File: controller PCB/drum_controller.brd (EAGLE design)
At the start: 160 x 100 mm, 1 part

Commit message: connected LED anode to +5V
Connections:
- new net +5V: LED1.A
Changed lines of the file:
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@@
 <contactref element="LED1" pad="K"/>
+</signal>
+<signal name="+5V">
+<contactref element="LED1" pad="A"/>
 </signal>
 </signals>

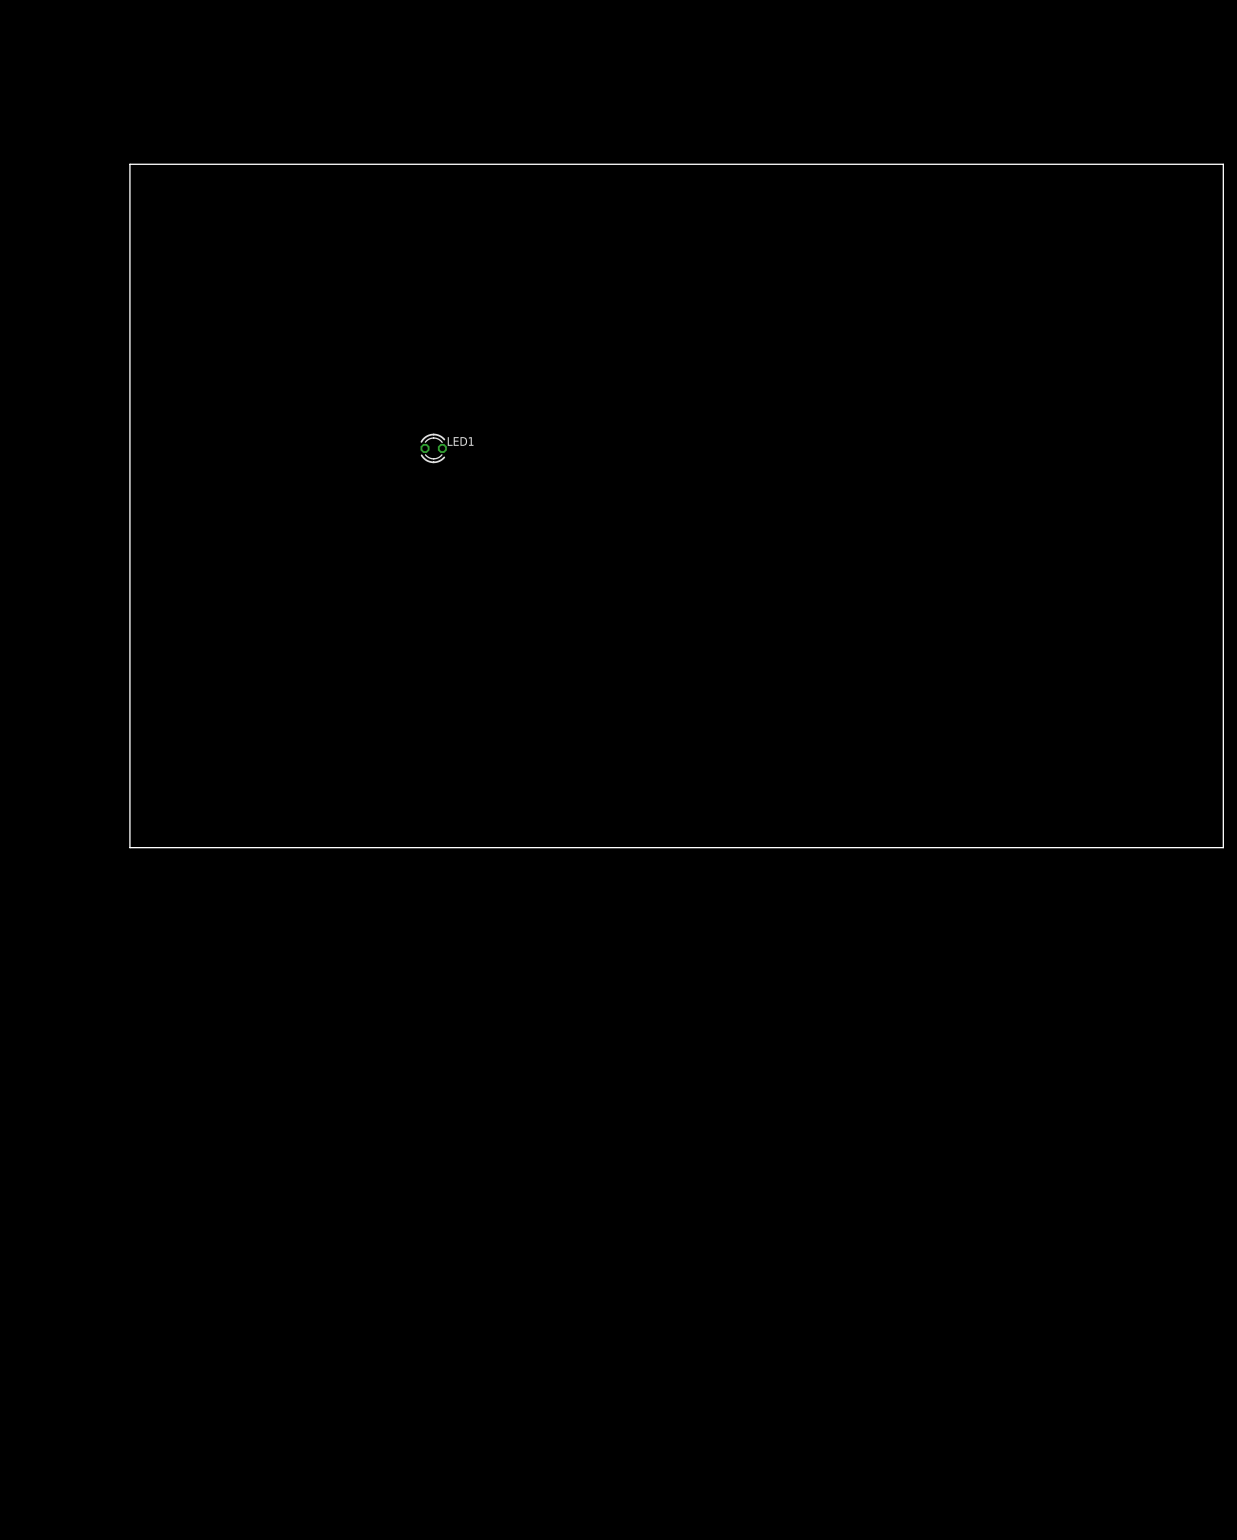
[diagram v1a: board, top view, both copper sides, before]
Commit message: added all 8 piezos to schematic, board not layed out yet
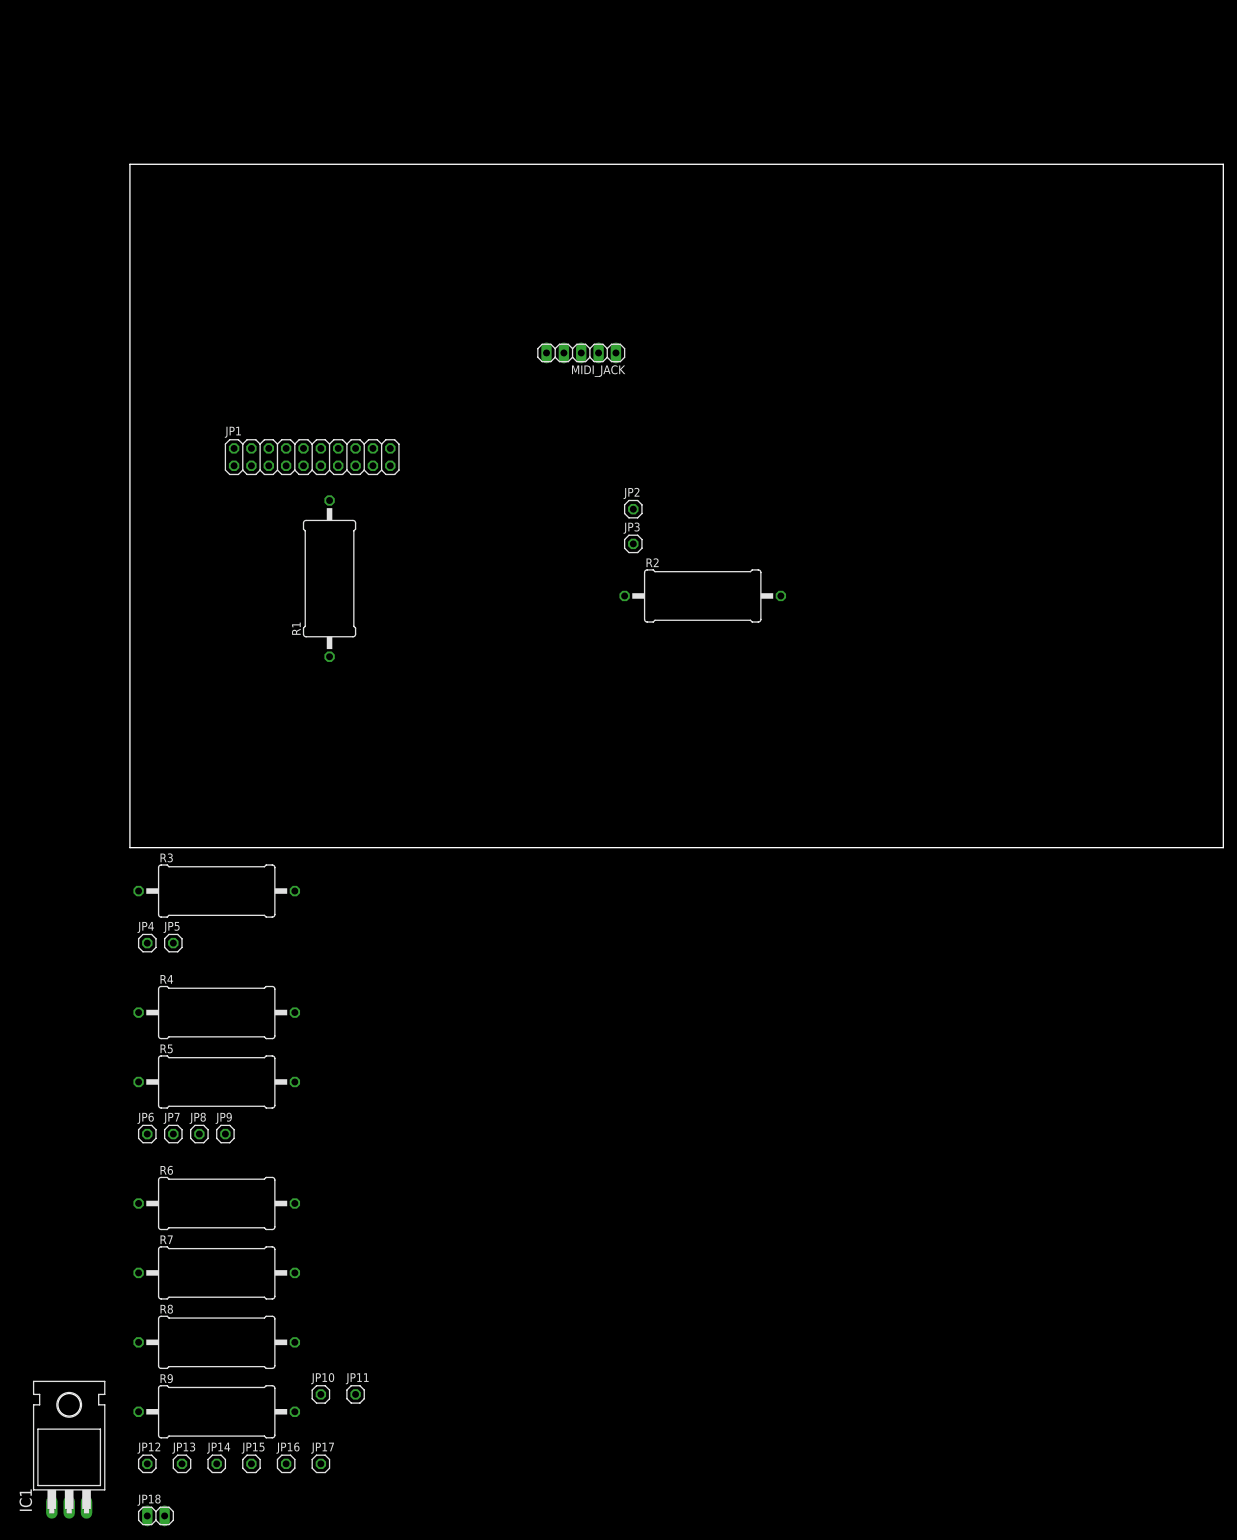
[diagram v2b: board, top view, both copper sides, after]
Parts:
- removed LED1: TLLY4400, led:LED3MM
- added IC1: 7805T, adafruit:TO220H
- added JP1: (no value), pinhead:2X10
- added JP10, JP12, JP14, JP16, JP2, JP4, JP6, JP8: P+, pinhead:1X01
- added JP11, JP13, JP15, JP17, JP3, JP5, JP7, JP9: P-, pinhead:1X01
- added JP18: (no value), pinhead:1X02
- added MIDI_JACK: (no value), pinhead:1X05
- added R1: 220, rcl:P0817/22
- added R2, R3, R4, R5, R6, R7, R8, R9: 1M, rcl:P0817/22
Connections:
- new net 12V: IC1.1, JP18.1
- new net A0: JP1.5, JP2.1, R2.2
- new net A1: JP1.7, JP4.1, R3.2
- new net A2: JP1.9, JP6.1, R4.2
- new net A3: JP1.11, JP8.1, R5.2
- new net A4: JP1.13, JP10.1, R6.2
- new net A5: JP1.15, JP12.1, R7.2
- new net A6: JP1.17, JP14.1, R8.2
- new net A7: JP1.2, JP16.1, R9.2
- new net N$1: MIDI_JACK.4, R1.1
- new net TXD: JP1.3, MIDI_JACK.2
- net +5V: now also IC1.3, JP1.1, R1.2; no longer LED1.A
- net GND: now also IC1.2, JP1.19, JP11.1, JP13.1, JP15.1, JP17.1, JP18.2, JP3.1, JP5.1, JP7.1, JP9.1, MIDI_JACK.3, R2.1, R3.1, R4.1, R5.1, R6.1, R7.1, R8.1, R9.1; no longer LED1.K

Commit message: resized PCB to match Hammond 1898 enclosure (notches need to be completed)
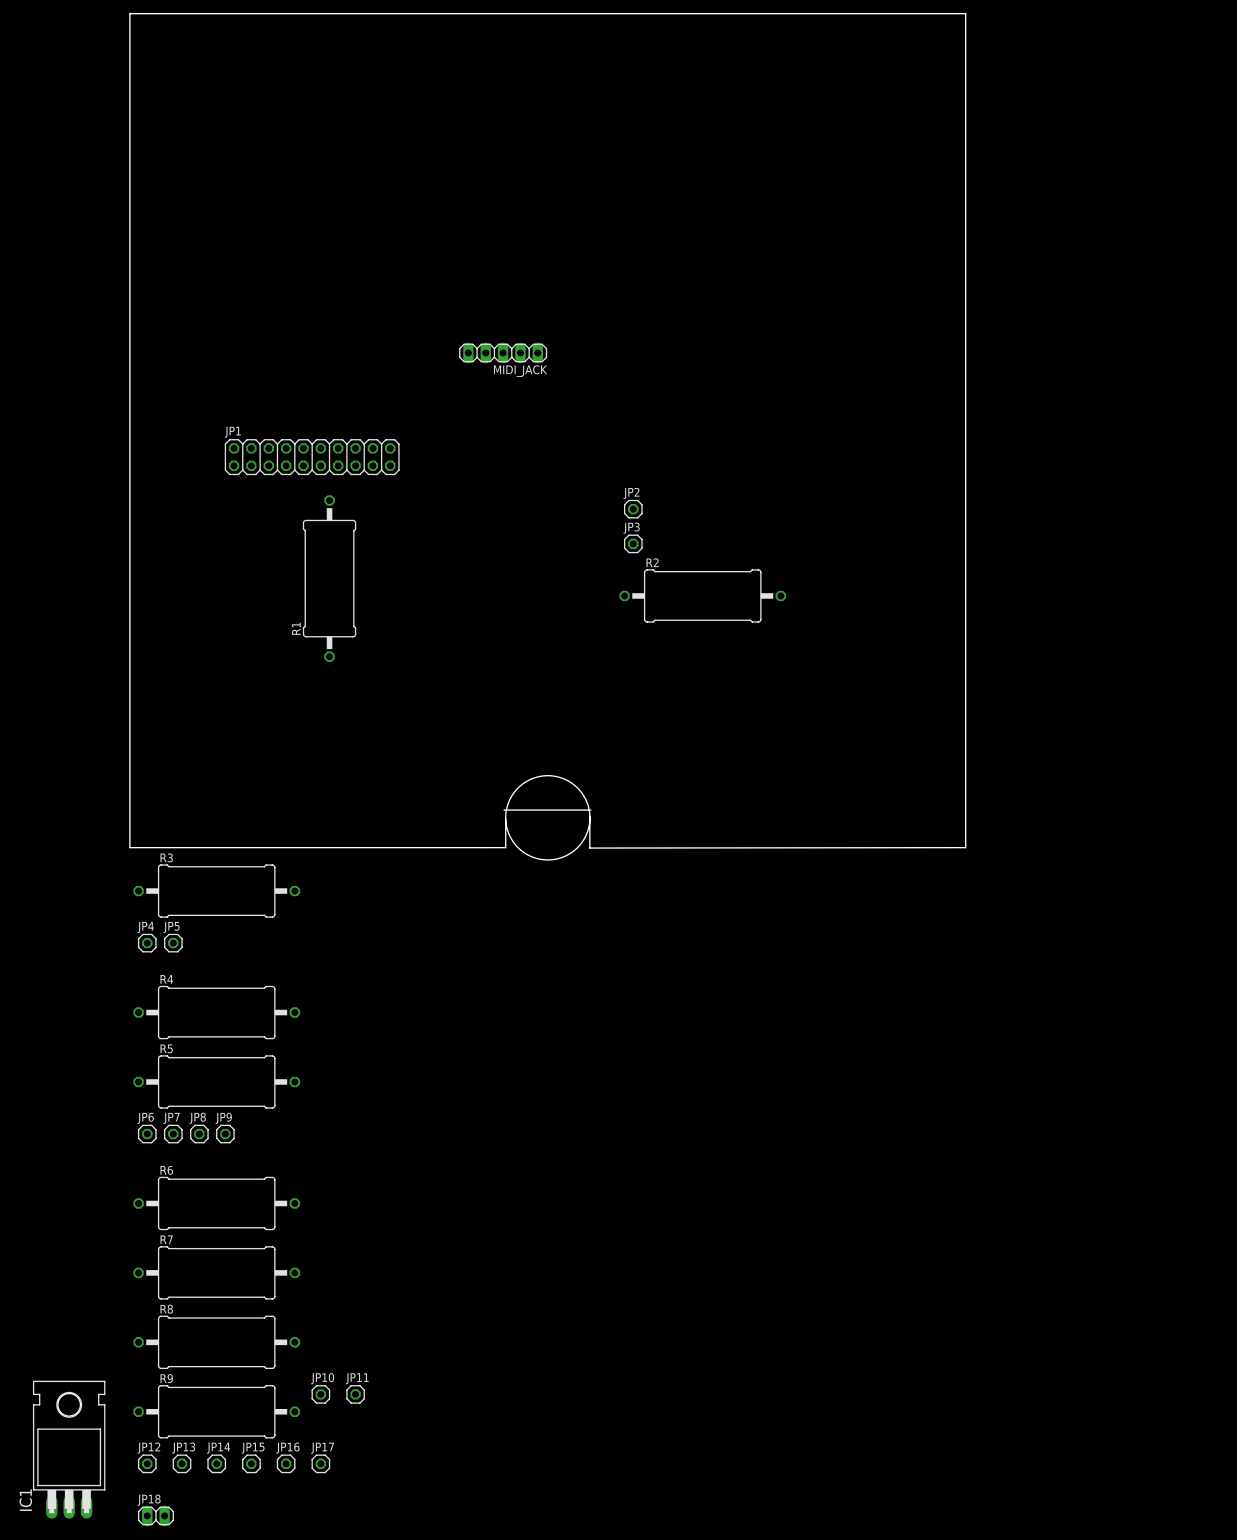
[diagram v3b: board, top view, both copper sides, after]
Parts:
- moved MIDI_JACK 11.4 mm to (54.6, 72.4)
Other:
- board size 160 x 100 mm -> 122.3 x 123.8 mm
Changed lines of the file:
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@@
 <setting verticaltext="up"/>
 </settings>
-<grid distance="50" unitdist="mil" unit="mil" style="lines" multiple="1" display="no" altdistance="5" altunitdist="mil" altunit="mil"/>
+<grid distance="50" unitdist="mil" unit="mm" style="lines" multiple="1" display="yes" altdistance="0.1" altunitdist="mm" altunit="mm"/>
 <layers>
 <layer number="1" name="Top" color="4" fill="1" visible="yes" active="yes"/>
@@
 <board>
 <plain>
-<wire x1="0" y1="0" x2="160" y2="0" width="0" layer="20"/>
-<wire x1="160" y1="0" x2="160" y2="100" width="0" layer="20"/>
-<wire x1="160" y1="100" x2="0" y2="100" width="0" layer="20"/>
-<wire x1="0" y1="100" x2="0" y2="0" width="0" layer="20"/>
+<wire x1="0" y1="0" x2="52.07" y2="0" width="0" layer="20"/>
+<wire x1="52.07" y1="0" x2="54.99" y2="0" width="0" layer="20"/>
+<wire x1="67.3" y1="-0.06" x2="122.3" y2="0" width="0" layer="20"/>
+<wire x1="122.3" y1="0" x2="122.3" y2="122.04" width="0" layer="20"/>
+<wire x1="122.3" y1="122.04" x2="0" y2="122.04" width="0" layer="20"/>
+<wire x1="0" y1="122.04" x2="0" y2="0" width="0" layer="20"/>
+<circle x="61.15" y="4.365" radius="6.165" width="0.1524" layer="20"/>
+<wire x1="67.31" y1="4.58" x2="67.3" y2="-0.06" width="0.1524" layer="20"/>
+<wire x1="54.99" y1="4.18" x2="54.99" y2="0" width="0.1524" layer="20"/>
+<wire x1="54.75" y1="5.5" x2="67.45" y2="5.5" width="0.1524" layer="20"/>
 </plain>
 <attributes>
@@
 <elements>
 <element name="JP1" library="pinhead" package="2X10" value="" x="26.67" y="57.15"/>
-<element name="MIDI_JACK" library="pinhead" package="1X05" value="" x="66.04" y="72.39" rot="R180"/>
+<element name="MIDI_JACK" library="pinhead" package="1X05" value="" x="54.61" y="72.39" rot="R180"/>
 <element name="R1" library="rcl" package="P0817/22" value="220" x="29.21" y="39.37" rot="R90"/>
 <element name="JP2" library="pinhead" package="1X01" value="P+" x="73.66" y="49.53"/>
@@
 <contactref element="JP18" pad="2"/>
 <contactref element="IC1" pad="2"/>
-<wire x1="73.66" y1="44.45" x2="66.04" y2="72.39" width="0" layer="19" extent="1-1"/>
+<wire x1="73.66" y1="44.45" x2="54.61" y2="72.39" width="0" layer="19" extent="1-1"/>
 <wire x1="72.39" y1="36.83" x2="73.66" y2="44.45" width="0" layer="19" extent="1-1"/>
-<wire x1="38.1" y1="55.88" x2="66.04" y2="72.39" width="0" layer="19" extent="1-1"/>
+<wire x1="38.1" y1="55.88" x2="54.61" y2="72.39" width="0" layer="19" extent="1-1"/>
 <wire x1="1.27" y1="-6.35" x2="38.1" y2="55.88" width="0" layer="19" extent="1-1"/>
 <wire x1="6.35" y1="-13.97" x2="1.27" y2="-6.35" width="0" layer="19" extent="1-1"/>
@@
 <contactref element="MIDI_JACK" pad="4"/>
 <contactref element="R1" pad="1"/>
-<wire x1="29.21" y1="27.94" x2="63.5" y2="72.39" width="0" layer="19" extent="1-1"/>
+<wire x1="29.21" y1="27.94" x2="52.07" y2="72.39" width="0" layer="19" extent="1-1"/>
 </signal>
 <signal name="TXD">
 <contactref element="JP1" pad="3"/>
 <contactref element="MIDI_JACK" pad="2"/>
-<wire x1="17.78" y1="55.88" x2="68.58" y2="72.39" width="0" layer="19" extent="1-1"/>
+<wire x1="17.78" y1="55.88" x2="57.15" y2="72.39" width="0" layer="19" extent="1-1"/>
 </signal>
 <signal name="A0">
